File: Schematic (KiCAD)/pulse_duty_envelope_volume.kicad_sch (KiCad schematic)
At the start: 74 parts, among them J65 Reg 4 D-Latch N, J68 Counter 4 Reset CL3

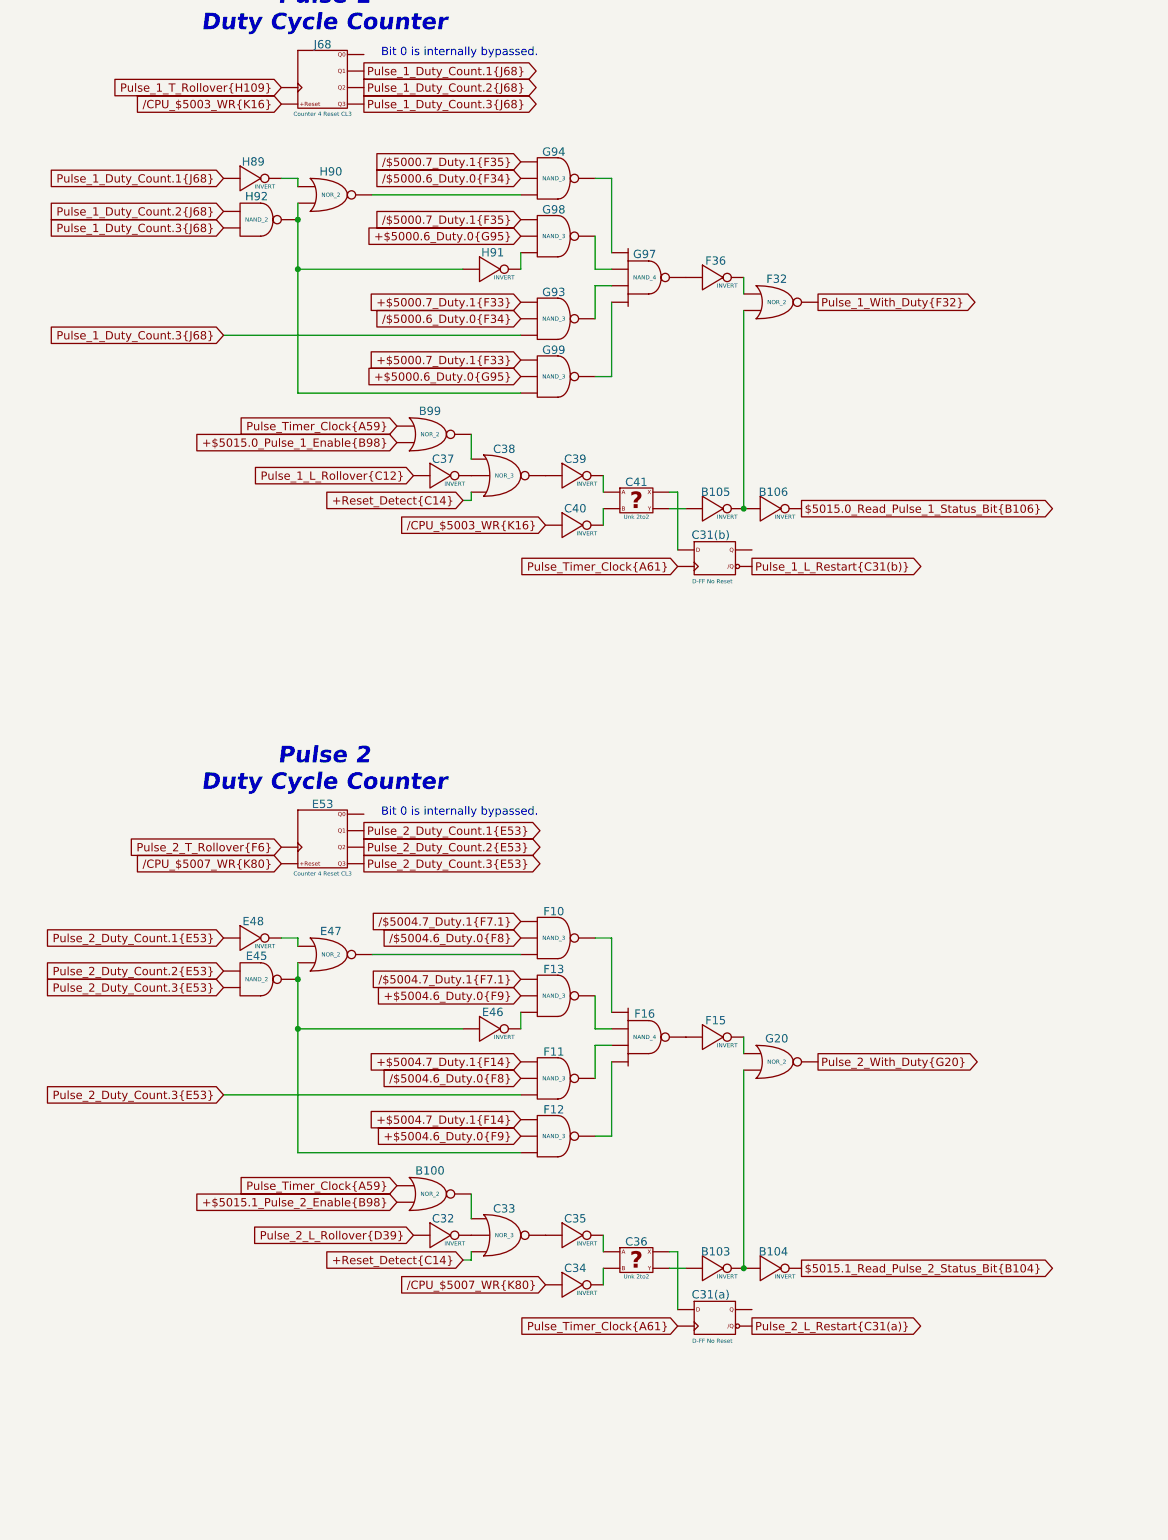
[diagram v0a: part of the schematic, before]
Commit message: - Lots of additional comments and signal name improvements.  - "Don't know what this is yet but it is important" section of the pulse channels:    - I worked out the logic and it is a 4-bit binary up-counter with preload, made from gates and D-latches instead of T-flip-flops.    - It is extremely similar to the envelope counter, but takes twice the die space and much more traces.    - None of its outputs go anywhere else, so I believe that it has no actual function.    - It seems to be a previous attempt at making the envelope counter and it got disconnected and left in.    - Each pulse channel has its own copy and I moved both of them to the "Artifacts" sheet.    - The wasted space amounts to about half of one of the large columns on the left side of the die.  - A couple of "OAI2" cells that noted "unclear order": I determined the correct order of the inputs based on several others which were known.  - Deduced the purpose of the 2 separate methods of scanline detection:    - The one looking for 3 consecutive reads finds the start of a scanline.    - The one counting PPU /RD to find PPU cycle 336, finds the end of the scanline.    - I moved these beside each other on the same sheet for clarity.  - A66.5 Changed from Nand to Nor in order to make sense.  - Basic test mode:    - Pin 92: Active low, enables test mode.    - Pin 29: In test mode, it gives external control of "Scanline Start Detection", which is normally done with the familiar 3 matching PPU reads.  When not in test mode, the pin has no function.    - Pin 30: In test mode, it gives external control of "Scanline End Detection", which is normally done by counting PPU /RD to find PPU cycle 336.  It also gives control of "Pulse Length Clock" when in test mode.  When not in test mode, the pin has no function.    - Pin 98/SL3: In test mode, it gives external control of "Pulse Timer Clock".  Whether or not in test mode, this pin low makes the MMC5 pretend $5104 had not yet been written since reset, probably as a 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
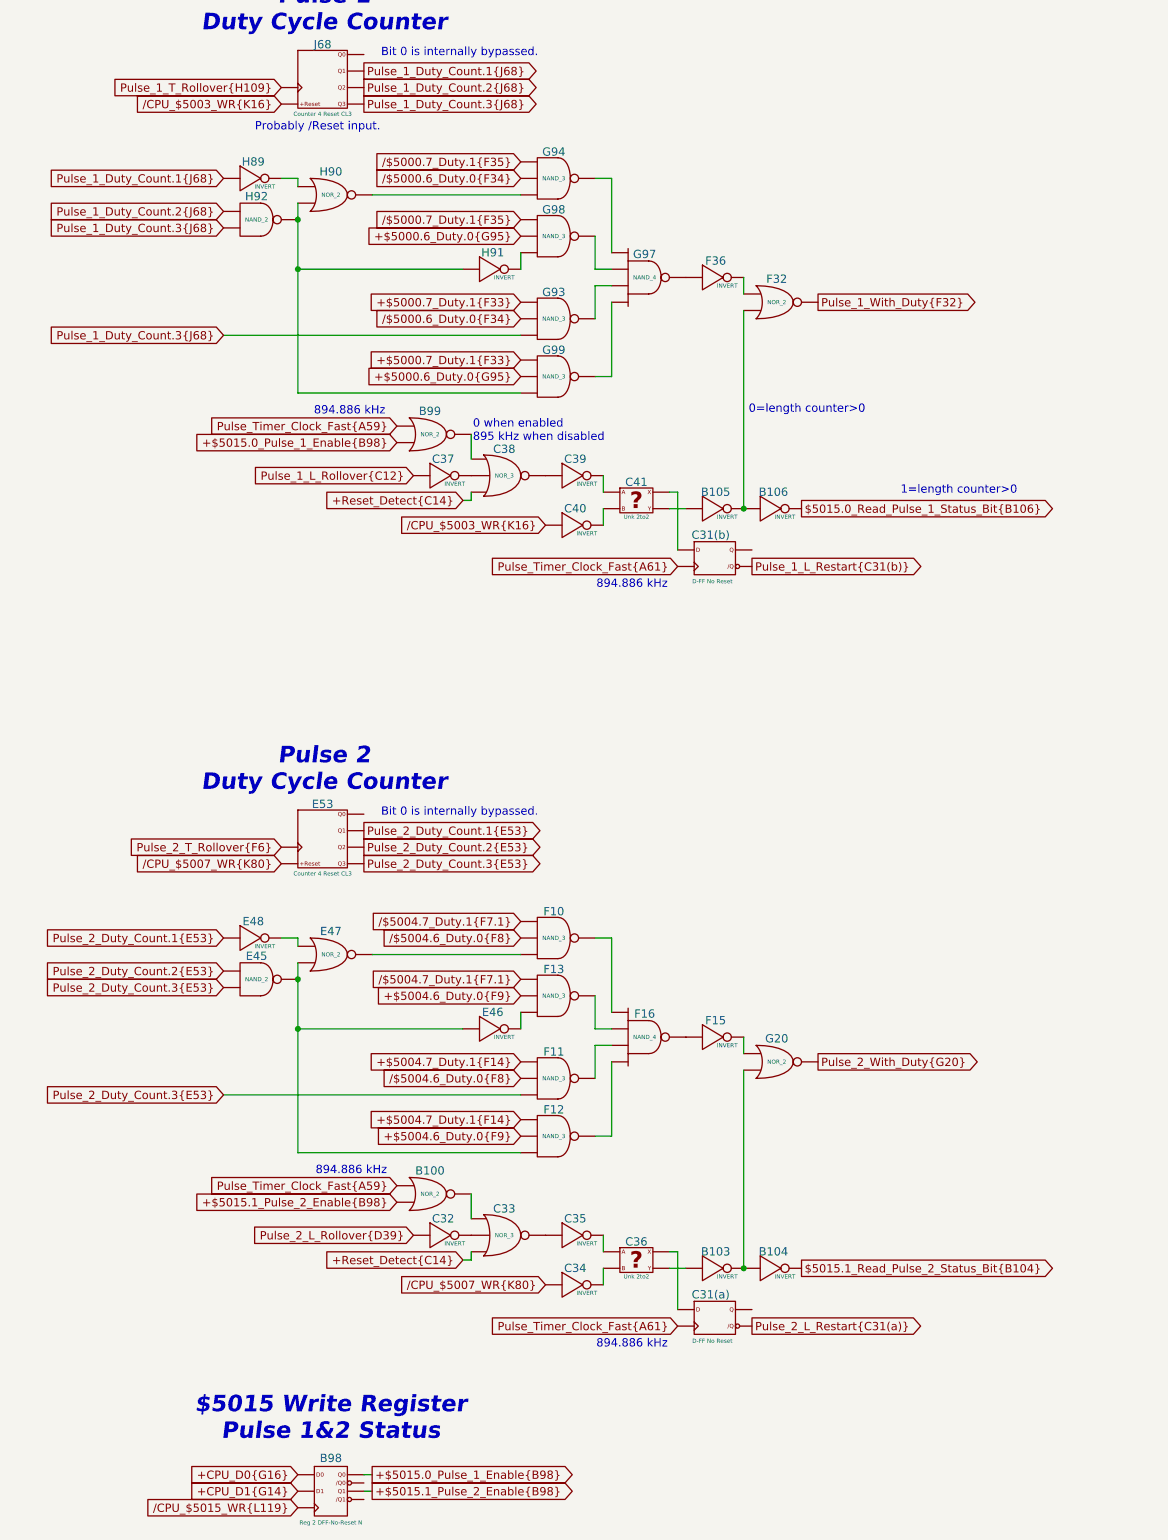
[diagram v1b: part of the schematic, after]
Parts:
- added B98: Reg 2 DFF-No-Reset N, symbol MMC5:Reg_2_DFF-No-Reset_N
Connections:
- net Pulse_Timer_Clock{A59} is gone; now on net Pulse_Timer_Clock_Fast{A59}: B100. (X), B99. (X)
- net Pulse_Timer_Clock{A61} is gone; now on net Pulse_Timer_Clock_Fast{A61}: C31(a). (/Q), C31(b). (/Q)
- net +$5015.0_Pulse_1_Enable{B98}: now also B98. (/Q1)
- net +$5015.1_Pulse_2_Enable{B98}: now also B98. (/Q1)
- net +CPU_D0{G16}: now also B98. (/Q1)
- net +CPU_D1{G14}: now also B98. (/Q1)
- net Pulse_Timer_Clock_Fast{A59}: now reaches B99. (X)
- net Pulse_Timer_Clock_Fast{A59}: no longer C38. (X)
- net at H90. (X): now also G94. (X); no longer H89. (X)
- net at C36. (Y): now also B103. (X); no longer C34. (X)
- net at C35. (X): now also C33. (X); no longer C36. (Y)
- net Pulse_Timer_Clock_Fast{A61}: now reaches C31(a). (/Q)
- net Pulse_Timer_Clock_Fast{A61}: no longer C36. (Y)
- net at B103. (X): now also B104. (X), G20. (X); no longer C36. (Y)
- net at F36. (X): now also G97. (X); no longer F32. (X)
- net at C39. (X): now also C38. (X); no longer C41. (Y)
- net at E47. (X): now also F10. (X); no longer E48. (X)
- net at F15. (X): now also F16. (X); no longer G20. (X)
- net at G97. (X): now also G99. (X); no longer G98. (X)
- net at C41. (Y): now also C31(b). (/Q); no longer C40. (X)
- net at F16. (X): now also F13. (X); no longer F11. (X)
- new net: E45. (X), E46. (X), E47. (X), F12. (X)
- new net: F19. (X), F23. (X)
- new net: B99. (X), C38. (X)
- new net: H89. (X), H90. (X)
- new net: G99. (X), H90. (X), H91. (X), H92. (X)
- new net: C34. (X), C36. (Y)
- new net: C35. (X), C36. (Y)
- new net: C31(a). (/Q), C36. (Y)
- new net: H101. (X), H105. (X)
- new net: H100. (X), H104. (X)
- new net: F20. (X), F24. (X)
- new net: F32. (X), F36. (X)
- new net: B105. (X), B106. (X), F32. (X)
- new net: F35. (X), G85. (/Q3)
- new net: F34. (X), G85. (/Q3)
- new net: C39. (X), C41. (Y)
- new net: E47. (X), E48. (X)
- new net: F18. (X), F22. (X)
- new net: C37. (X), C38. (X)
- new net: F15. (X), G20. (X)
- new net: G97. (X), G98. (X)
- new net: C40. (X), C41. (Y)
- new net: H103. (X), H107. (X)
- new net: C32. (X), C33. (X)
- new net: H102. (X), H106. (X)
- new net: F11. (X), F16. (X)
- new net: G93. (X), G97. (X)
- new net: F21. (X), F26. (X)
- new net: E68. (/Q3), F7.1. (X)
- new net: E68. (/Q3), F8. (X)
- new net: G94. (X), G97. (X)
- new net: F10. (X), F16. (X)
- new net: F12. (X), F16. (X)
- new net: B100. (X), C33. (X)
- new net /CPU_$5015_WR{L119}: B98. (/Q1)
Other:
- note added: "$5015 Write Register Pulse 1&2 Status"
- note added: "0 when enabled 895 kHz when disabled"
- note added: "0=length counter>0"
- note added: "1=length counter>0"
- note added: "894.886 kHz"
- note added: "Probably /Reset input."
